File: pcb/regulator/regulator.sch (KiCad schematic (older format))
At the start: 16 parts, among them J1 Conn_01x04, J2 Conn_01x03, SW1 SW_Push, U1 STM32G071CBT6, Y1 32kHz, Y2 8MHz

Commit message: Device Schematic v1
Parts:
- removed BT1: Battery_Cell, symbol Device:Battery_Cell
- removed C6: 20pF, symbol Device:C
- removed C7: 4,7uF, symbol Device:C
- removed J2: Conn_01x03, symbol Connector_Generic:Conn_01x03
- removed Y2: 8MHz, symbol Device:Crystal
- added C6: 4.7uF, symbol Device:CP
- added D1, D2, D3, D4, D5, D6: 1N5819, Diode_THT:D_DO-41_SOD81_P10.16mm_Horizontal, symbol Diode:1N5819
- added DS1: WC1602A, Display:WC1602A, symbol Display_Character:WC1602A
- added F1: 0.5 A, symbol Device:Fuse_Small
- added J2: Conn. 1x2, symbol Connector_Generic:Conn_01x02
- added J3: 3x1 Screw conn., symbol Connector:Screw_Terminal_01x03
- added K1: EC2-5TNU, Relay_THT:Relay_DPDT_Kemet_EC2_DoubleCoil, symbol Relay:EC2-5TNU
- added Q1, Q2, Q3, Q4, Q5, Q6, Q7, Q8: FDV303N, Package_TO_SOT_SMD:SOT-23, symbol things:FDV303N
- added R10, R13, R4: 100, symbol Device:R
- added R11, R12, R14, R15, R18, R19, R20, R21, R3, R6, R7, R8: 10k, symbol Device:R
- added R16, R2, R5, R9: 100k, symbol Device:R
- added R17: 200, symbol Device:R
- added RV1: 10k, symbol Device:R_POT
- added SW2: K1, symbol Switch:SW_Push
- added SW3: K2, symbol Switch:SW_Push
- added SW4: K3, symbol Switch:SW_Push
- added SW5: K4, symbol Switch:SW_Push
- added U2: U3V12F5, Connector_PinHeader_2.54mm:PinHeader_1x03_P2.54mm_Vertical_SMD_Pin1Left, symbol things:U3V12F5
- C3: value 20pF -> 33pF
- J1: value Conn_01x04 -> Prog. Connector
- R1: value 390R -> 100
- SW1: value SW_Push -> RESET
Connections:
- net GND: now also C5.1, C6.2, D4.2 (A), D5.2 (A), DS1.1 (VSS), DS1.10 (D3), DS1.16 (LED(-)), DS1.5 (R/W), DS1.7 (D0), DS1.8 (D1), DS1.9 (D2), J2.2 (Pin_2), Q2.2 (S), Q3.2 (S), R16.2, R2.1, R5.1, R9.1, RV1.1, SW2.2, SW3.2, SW4.2, SW5.2, U2.2 (GND); no longer C5.2
- net VDD: now also C5.2, C8.2, U1.4 (VBAT), U1.5 (VREF+), C6.1, D3.1 (K), Q1.3 (D), Q4.1 (G), Q5.1 (G), Q7.1 (G), Q8.1 (G), R11.1, R12.1, R18.1, R19.1, R3.1, R6.1, R7.1, R8.1; no longer C5.1
- net SWDIO: now reaches J1.4 (Pin_4), U1.35 (PA13)
- net SWCLK: now reaches J1.3 (Pin_3), U1.36 (PA14/BOOT0)
- net at U1.8 (PF0/OSC_IN): no longer C3.1
- net at U1.9 (PF1/OSC_OUT): no longer R1.2
- net at R1.1: now also Q2.1 (G), R2.2
- new net: Q1.1 (G), R4.1, R5.2
- new net: C3.1, D3.2 (A), Q1.2 (S), U2.1 (VIN)
- new net: D1.2 (A), D4.1 (K), K1.12, Q2.3 (D)
- new net: Q3.1 (G), R10.1, R9.2
- new net: D2.2 (A), D5.1 (K), K1.7, Q3.3 (D)
- new net: Q6.1 (G), R13.1, R16.1
- new net: DS1.15 (LED(+)), R17.1
- new net: D6.2 (A), Q6.2 (S), R17.2
- new net: DS1.3 (VO), RV1.2
- new net: F1.2, J2.1 (Pin_1)
- new net +5V: D1.1 (K), D2.1 (K), D6.1 (K), DS1.2 (VDD), K1.1, K1.6, Q6.3 (D), R14.1, R15.1, R20.1, R21.1, RV1.3, U2.3 (VOUT)
- new net BACKLIGHT: R13.2
- new net COM: J3.2 (Pin_2), K1.4
- new net EN_5V: R4.2
- new net KEY1: R3.2, SW2.1
- new net KEY2: R6.2, SW3.1
- new net KEY3: R7.2, SW4.1
- new net KEY4: R8.2, SW5.1
- new net LCD_D4: DS1.11 (D4)
- new net LCD_D4_HV: Q4.3 (D), R14.2
- new net LCD_D4_LV: Q4.2 (S), R11.2
- new net LCD_D5: DS1.12 (D5)
- new net LCD_D5_HV: Q5.3 (D), R15.2
- new net LCD_D5_LV: Q5.2 (S), R12.2
- new net LCD_D6: DS1.13 (D6)
- new net LCD_D6_HV: Q7.3 (D), R20.2
- new net LCD_D6_LV: Q7.2 (S), R18.2
- new net LCD_D7: DS1.14 (D7)
- new net LCD_D7_HV: Q8.3 (D), R21.2
- new net LCD_D7_LV: Q8.2 (S), R19.2
- new net LCD_EN: DS1.6 (E)
- new net LCD_RS: DS1.4 (RS)
- new net NC: J3.1 (Pin_1), K1.3
- new net NO: J3.3 (Pin_3), K1.5
- new net R_RESET: R10.2
- new net R_SET: R1.2
- new net VCC: F1.1
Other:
- note added: "Batt. 3.7 V or\nDC 3.7 V power supply"
- note added: "Display section"
- note added: "MCU\n"
- note added: "Power supply"
- note added: "Relay Control"
- note added: "User interface"
- moved on the sheet: C1, C2, C4, C5, C8, J1, SW1, U1, Y1

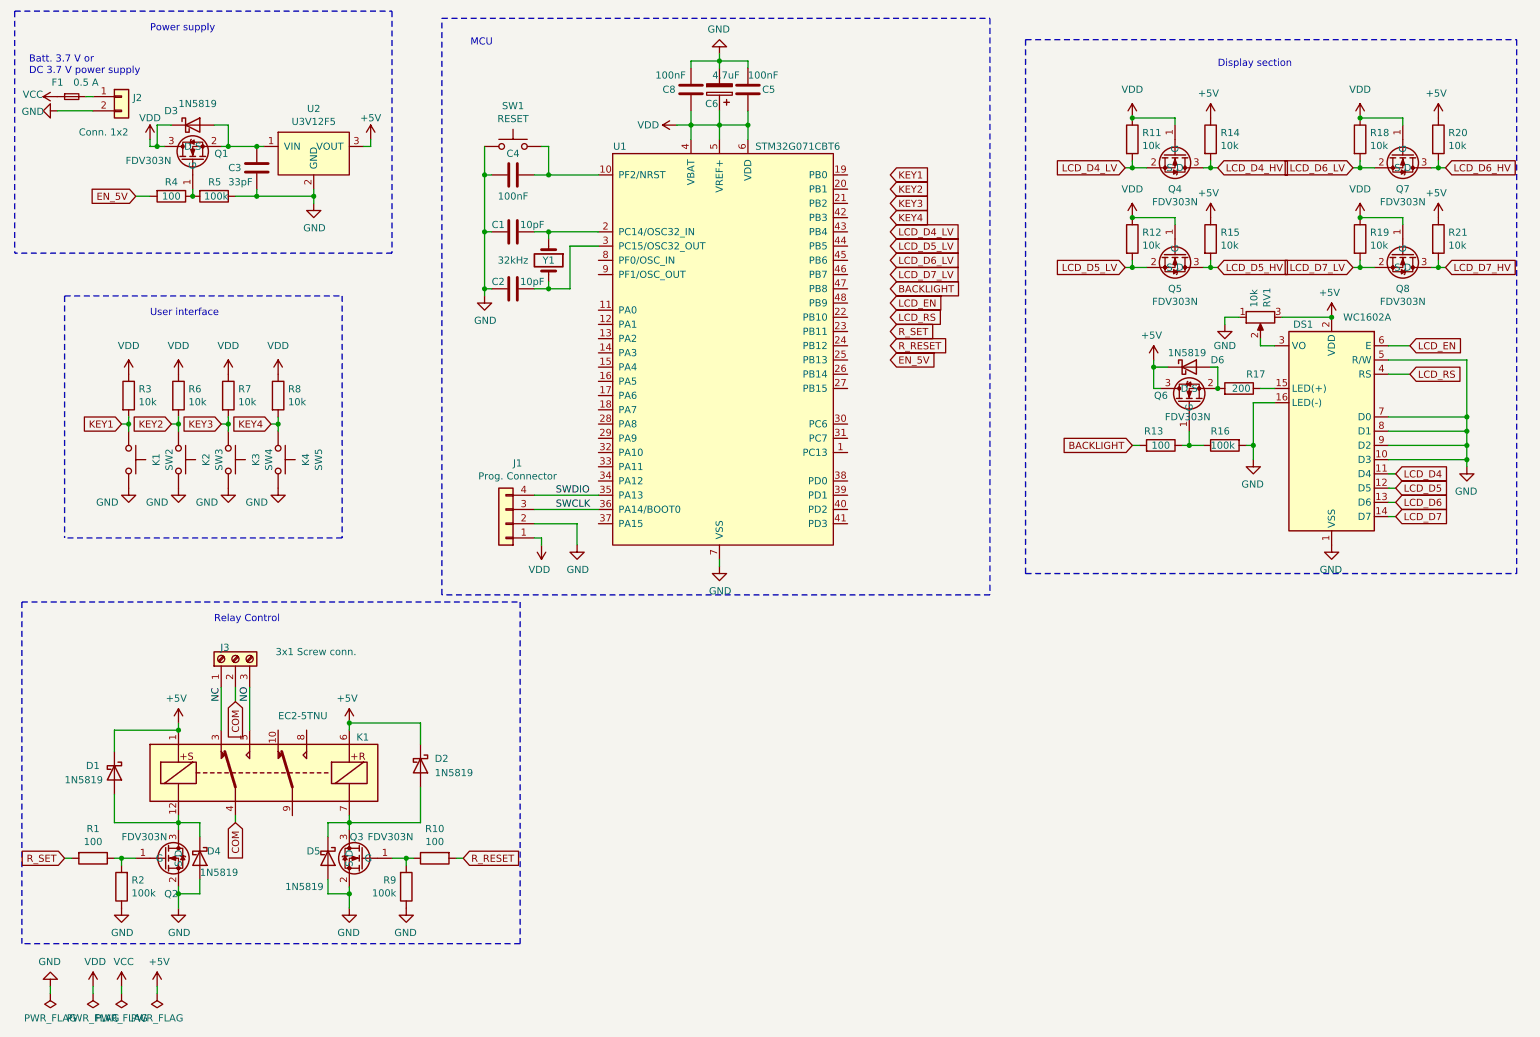
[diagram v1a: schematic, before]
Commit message: Schematic changes to improve reading
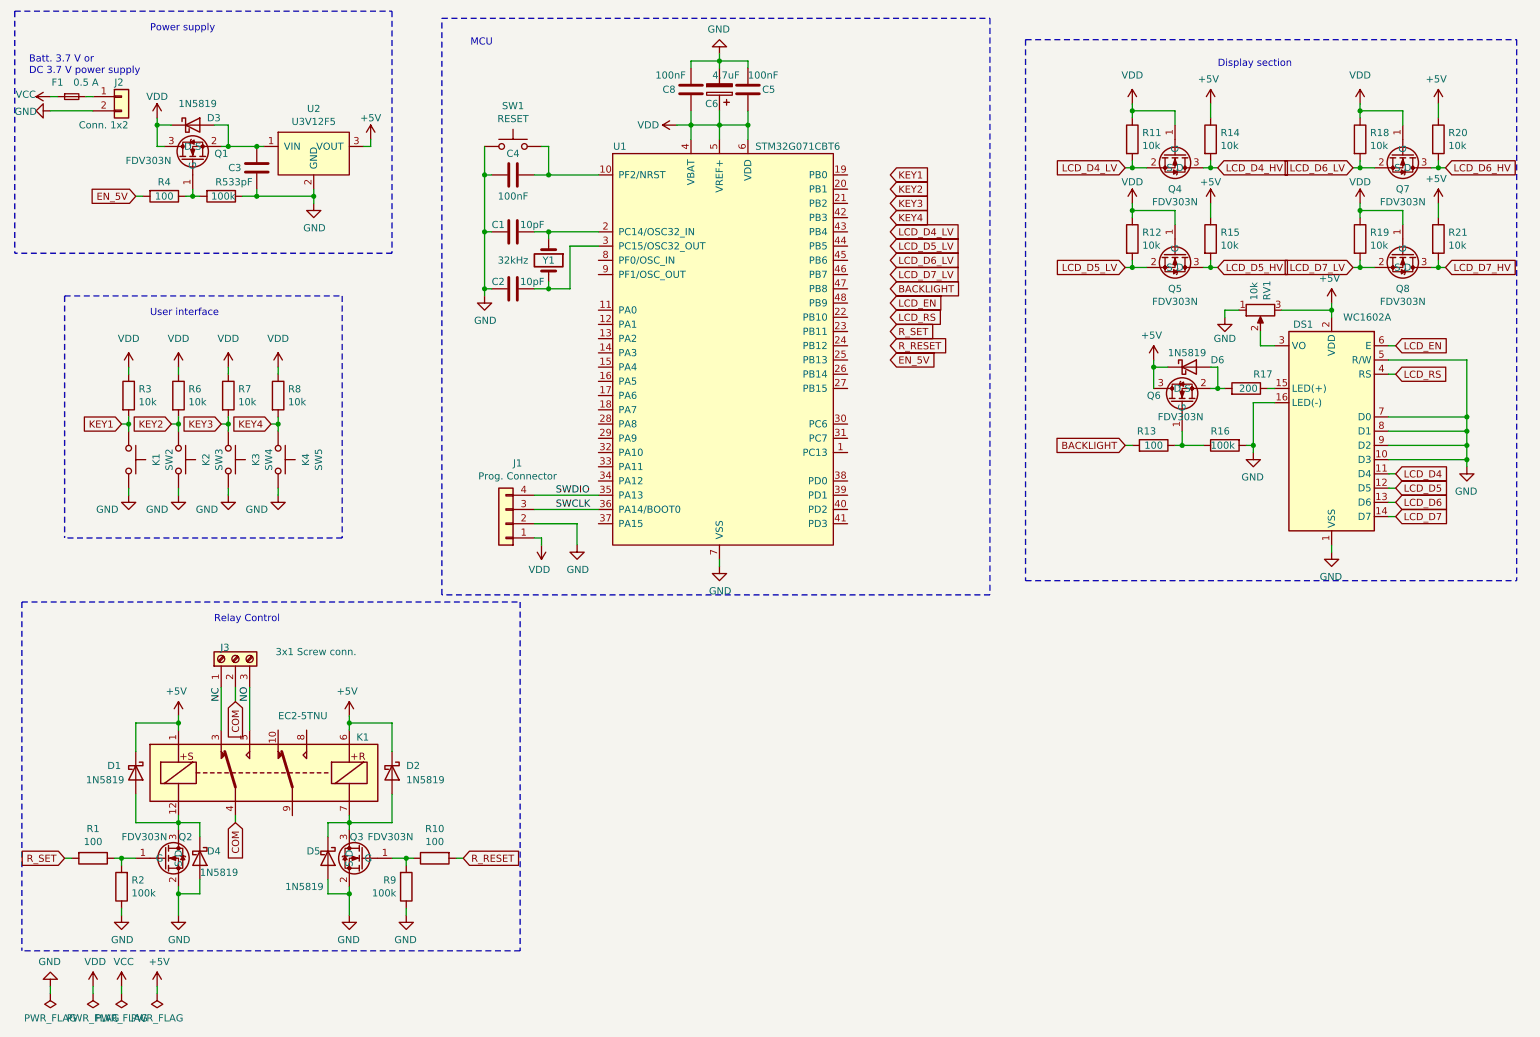
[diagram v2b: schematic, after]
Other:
- moved on the sheet: D1, D2, Q6, R13, R17, R4, R5, RV1

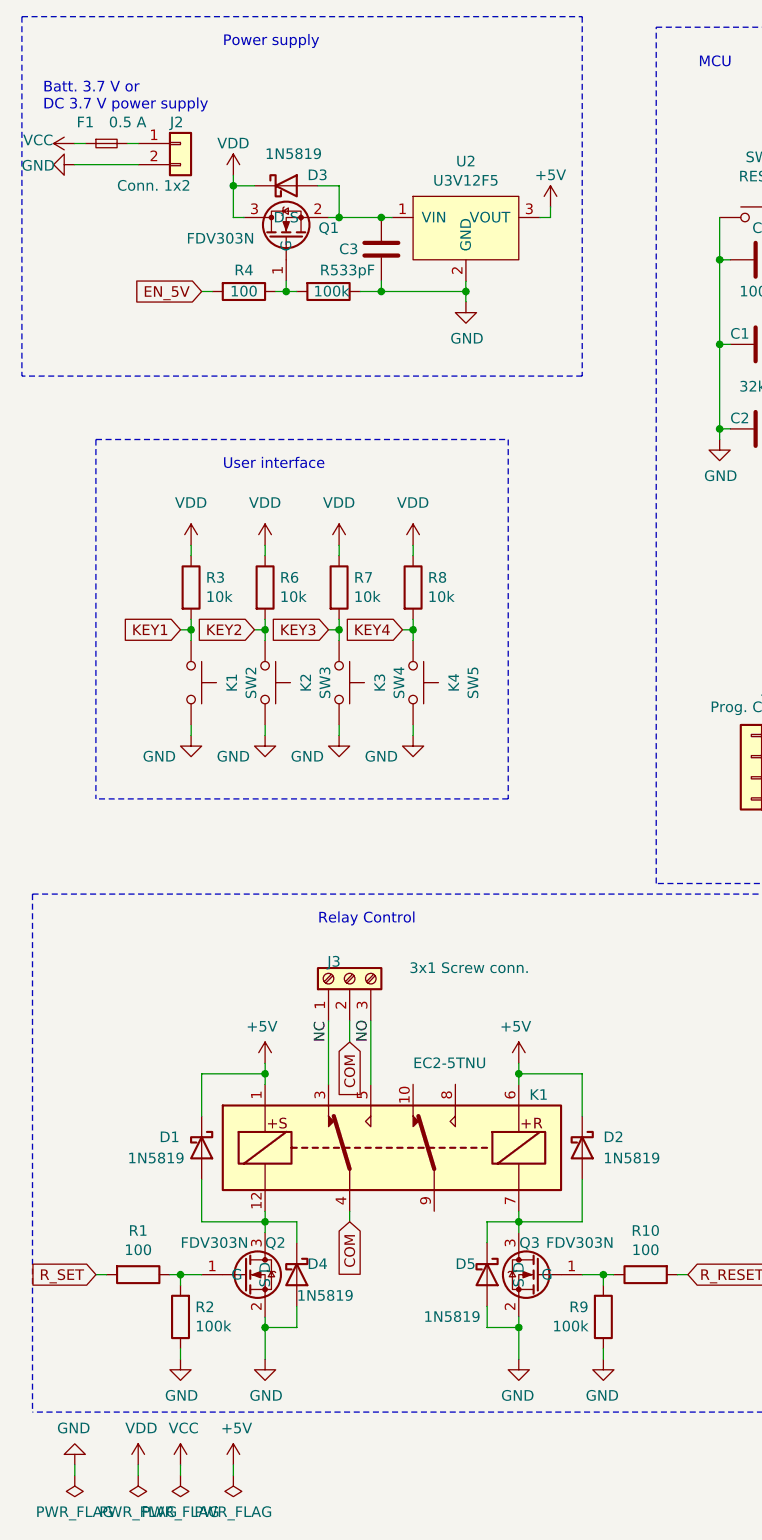
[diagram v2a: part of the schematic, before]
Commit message: Change MOSFET at 5V to proper one (P-MOSFET)
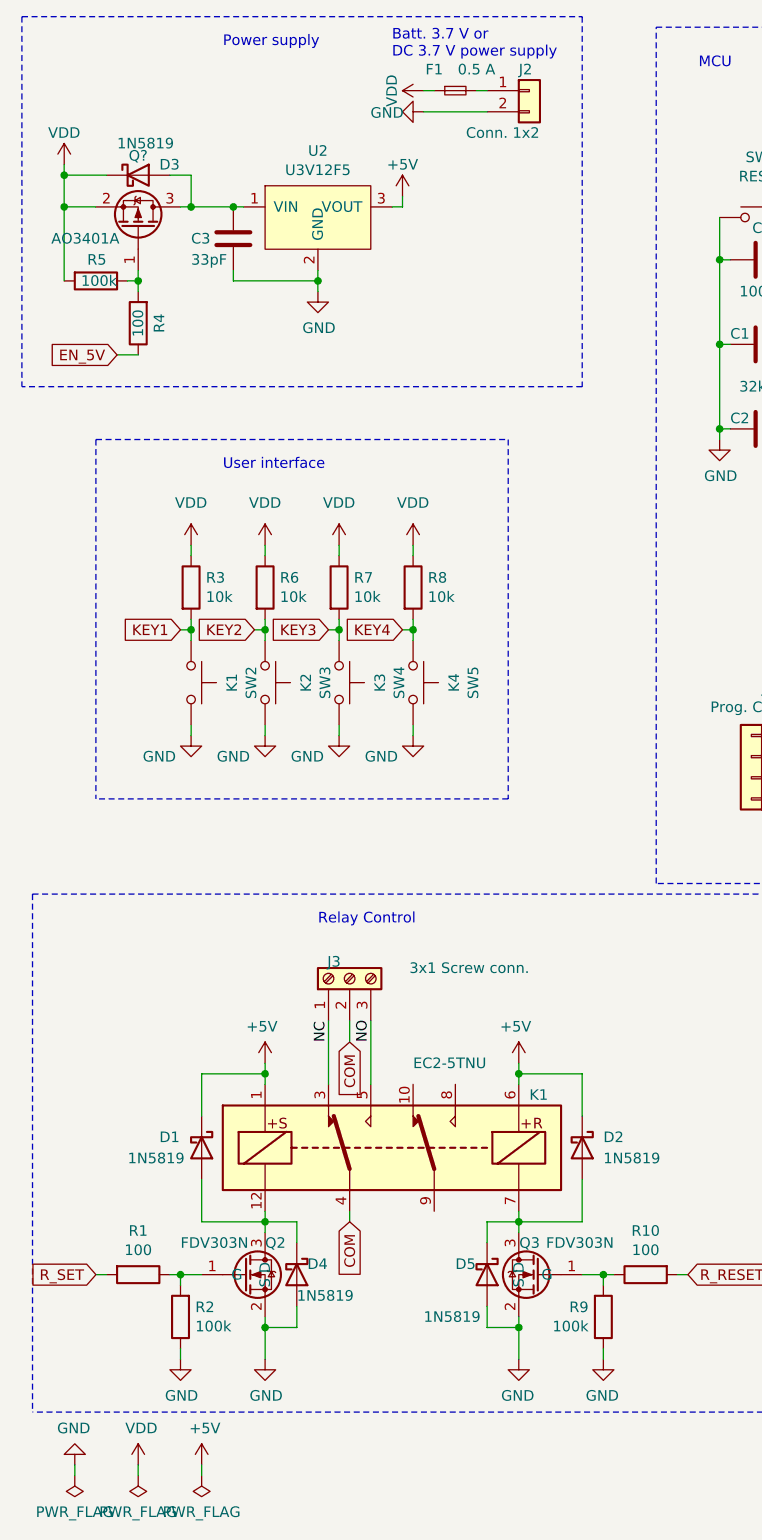
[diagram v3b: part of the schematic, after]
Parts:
- removed Q1: FDV303N, Package_TO_SOT_SMD:SOT-23, symbol things:FDV303N
- added Q?: AO3401A, Package_TO_SOT_SMD:SOT-23, symbol Transistor_FET:AO3401A
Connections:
- net VCC is gone; now on net VDD: F1.1
- net EN_5V: now also R4.1; no longer R4.2
- net GND: no longer R5.1
- net VDD: now also R5.2, Q?.2 (S)
- net at C3.1, D3.2 (A), U2.1 (VIN): now also Q?.3 (D)
- new net: Q?.1 (G), R4.2, R5.1
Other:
- moved on the sheet: C3, D3, F1, J2, R4, R5, U2
